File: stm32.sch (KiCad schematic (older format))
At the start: 39 parts, among them J1 USB_B_Micro, J2 Conn_02x05_Odd_Even, U1 STM32F767VITx, U5 LM2937, X1 8MHz

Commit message: manual sync & moving gerbers
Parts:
- added NT1, NT2: Net-Tie_2, rusEFI_Ola:Net-Tie_2_8.5mil, symbol Device:Net-Tie_2
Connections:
- net GND: now also NT2.2; no longer U1.36 (PB2)
- net PA9: now also NT1.2; no longer U1.68 (PA9)
- new net: NT2.1, U1.36 (PB2)
- new net: NT1.1, U1.68 (PA9)
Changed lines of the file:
@@
 Text Label 6250 3550 1    60   ~ 12
 VDD
-Text Label 7250 4750 0    60   ~ 12
+Text Label 7600 4750 0    60   ~ 12
 PA9
-Text Label 7250 4850 0    60   ~ 12
+Text Label 7600 4850 0    60   ~ 12
 PA10
-Text Label 7250 4950 0    60   ~ 12
+Text Label 7600 4950 0    60   ~ 12
 PA11
-Text Label 7250 5050 0    60   ~ 12
+Text Label 7600 5050 0    60   ~ 12
 PA12
 Wire Wire Line
@@
 	6600 2000 6600 2200
 Wire Wire Line
-	7250 5750 7950 5750
+	7250 5750 7600 5750
 Wire Wire Line
 	5100 5150 4850 5150
@@
 	6250 3550 6150 3550
 Connection ~ 6150 3550
+$Comp
+L Device:Net-Tie_2 NT2
+U 1 1 5D85D17A
+P 7700 5750
+F 0 "NT2" H 7700 5839 50  0000 C CNN
+F 1 "Net-Tie_2" H 7700 5840 50  0001 C CNN
+F 2 "rusEFI_Ola:Net-Tie_2_8.5mil" H 7700 5750 50  0001 C CNN
+F 3 "~" H 7700 5750 50  0001 C CNN
+	1    7700 5750
+	1    0    0    -1
+$EndComp
+Wire Wire Line
+	7800 5750 7950 5750
+Wire Wire Line
+	7250 4850 7600 4850
+Wire Wire Line
+	7250 4950 7600 4950
+Wire Wire Line
+	7250 5050 7600 5050
+Wire Wire Line
+	7250 4750 7300 4750
+$Comp
+L Device:Net-Tie_2 NT1
+U 1 1 5D86F689
+P 7400 4750
+F 0 "NT1" H 7400 4700 50  0000 C CNN
+F 1 "Net-Tie_2" H 7400 4840 50  0001 C CNN
+F 2 "rusEFI_Ola:Net-Tie_2_8.5mil" H 7400 4750 50  0001 C CNN
+F 3 "~" H 7400 4750 50  0001 C CNN
+	1    7400 4750
+	1    0    0    -1
+$EndComp
+Wire Wire Line
+	7500 4750 7600 4750
 $EndSCHEMATC

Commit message: Created LED footprint which better matches the MFG's suggested footprint, as well it includes a clear polarity indicator. https://github.com/rusefi/hw_microRusEfi/issues/81 Changed VVT, injector, and coil LED's to turn on when the device is being driven. https://github.com/rusefi/hw_microRusEfi/issues/82
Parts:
- D19: footprint LED_SMD:LED_0603_1608Metric -> rusEFI_Ola:LED-0603-rusEFI
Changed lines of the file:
@@
 Sheet 6 7
 Title "microRusEfi"
-Date "2019-07-01"
-Rev "R0.2"
+Date "2019-07-09"
+Rev "R0.2.1"
 Comp ""
 Comment1 ""
@@
 F 0 "D19" H 15400 3300 50  0000 C CNN
 F 1 "LED-RED" H 15300 3500 50  0000 C CNN
-F 2 "LED_SMD:LED_0603_1608Metric" H 15400 3400 60  0001 C CNN
+F 2 "rusEFI_Ola:LED-0603-rusEFI" H 15400 3400 60  0001 C CNN
 F 3 "" H 15400 3400 60  0000 C CNN
 F 4 "LTST-S270KRKT" H 0   0   50  0001 C CNN "Part #"

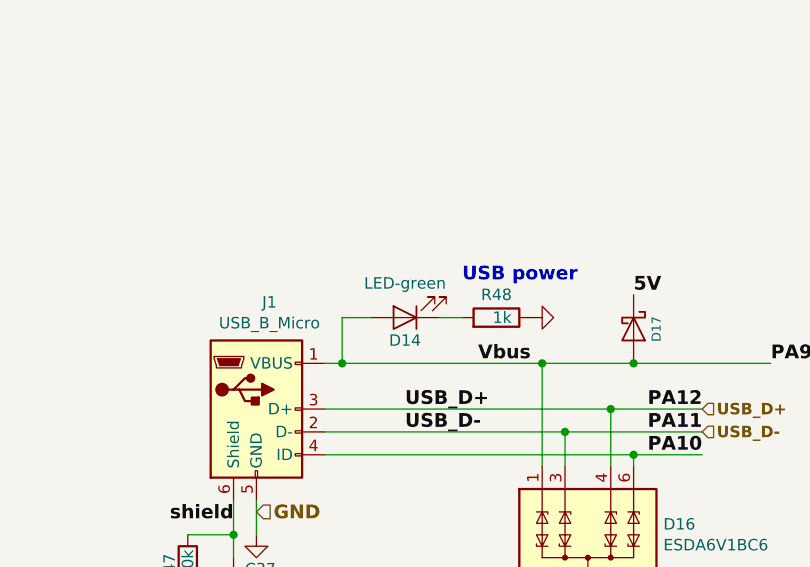
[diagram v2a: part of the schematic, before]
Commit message: Updated 1k/1.5k resistor arrays, updated 2.7k's and R141. Changed several K's into k's for consistent ref designation names. https://github.com/rusefi/hw_microRusEfi/issues/51
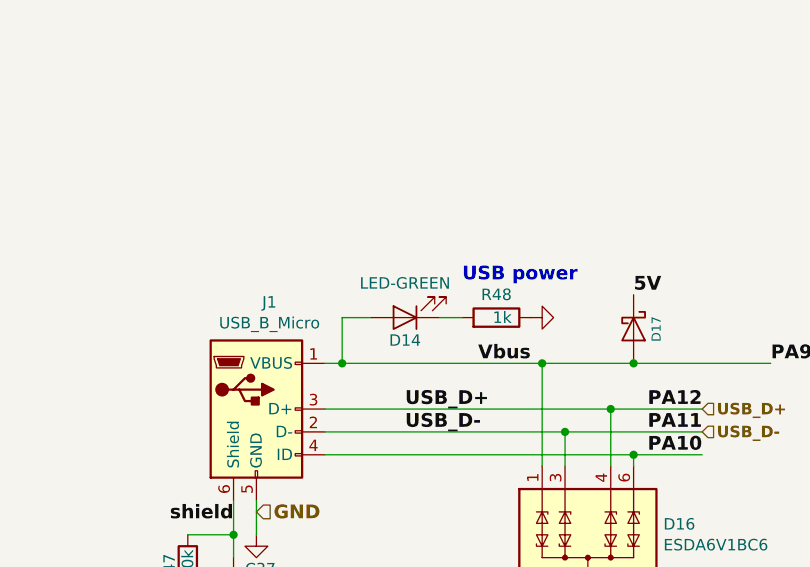
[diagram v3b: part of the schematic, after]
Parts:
- D14: value LED-green -> LED-GREEN
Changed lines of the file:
@@
 P 12150 3800
 F 0 "D14" H 12150 3900 50  0000 C CNN
-F 1 "LED-green" H 12150 3650 50  0000 C CNN
+F 1 "LED-GREEN" H 12150 3650 50  0000 C CNN
 F 2 "Capacitor_SMD:C_0603_1608Metric_Pad1.05x0.95mm_HandSolder" V 5   1700 60  0001 C CNN
 F 3 "" H 12150 3800 60  0001 C CNN
@@
 F 1 "10k" V 4050 3850 50  0000 C CNN
 F 2 "Resistor_SMD:R_0603_1608Metric" V 6380 6150 60  0001 C CNN
-F 3 "" H 9900 6175 60  0001 C CNN
+F 3 "TBD" H 9900 6175 60  0001 C CNN
 F 4 "RMCF0603JT10K0" H 0   0   50  0001 C CNN "Part #"
 F 5 "DIGI" H 0   0   50  0001 C CNN "VEND"
@@
 F 1 "10k" V 4650 4200 50  0000 C CNN
 F 2 "Resistor_SMD:R_0603_1608Metric" V 6980 6500 60  0001 C CNN
-F 3 "" H 10500 6525 60  0001 C CNN
+F 3 "TBD" H 10500 6525 60  0001 C CNN
 F 4 "RMCF0603JT10K0" H 0   0   50  0001 C CNN "Part #"
 F 5 "DIGI" H 0   0   50  0001 C CNN "VEND"

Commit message: new xtal 0.3
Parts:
- X1: footprint Crystal:Crystal_SMD_5032-2Pin_5.0x3.2mm -> Crystal_SMD_HC49-SD; Manufacturer NDK -> Abracon; Part # NX3225GD-8MHZ-STD-CRA-3 -> ABLS-8.000MHZ-B2-T; VEND# 644-1178-1-ND -> 535-9089-1-ND
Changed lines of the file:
@@
 F 0 "X1" H 4850 5450 60  0000 C CNN
 F 1 "8MHz" H 4850 5150 60  0000 C CNN
-F 2 "Crystal:Crystal_SMD_5032-2Pin_5.0x3.2mm" H 4850 5300 60  0001 C CNN
-F 3 "" H 4850 5300 60  0000 C CNN
+F 2 "Crystal_SMD_HC49-SD" H 4850 5300 60  0001 C CNN
+F 3 "" H 4850 5300 60  0001 C CNN
 F 4 "stm32f407_board" H 16200 4825 60  0001 C CNN "PageName"
 F 5 "DIGI" H -1800 1250 50  0001 C CNN "VEND"
-F 6 "NX3225GD-8MHZ-STD-CRA-3" H -1800 1250 50  0001 C CNN "Part #"
-F 7 "644-1178-1-ND" H -1800 1250 50  0001 C CNN "VEND#"
-F 8 "NDK" H 0   0   50  0001 C CNN "Manufacturer"
+F 6 "ABLS-8.000MHZ-B2-T" H -1800 1250 50  0001 C CNN "Part #"
+F 7 "535-9089-1-ND" H -1800 1250 50  0001 C CNN "VEND#"
+F 8 "Abracon " H 0   0   50  0001 C CNN "Manufacturer"
 	1    4850 5300
 	0    -1   -1   0

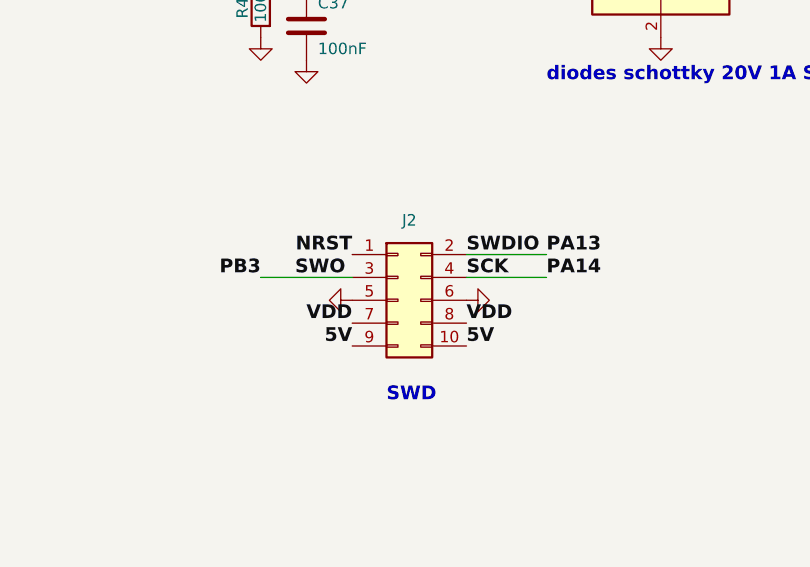
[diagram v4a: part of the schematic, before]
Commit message: Changed SWD connector to reflect validated brain board. https://github.com/rusefi/hw_microRusEfi/issues/88
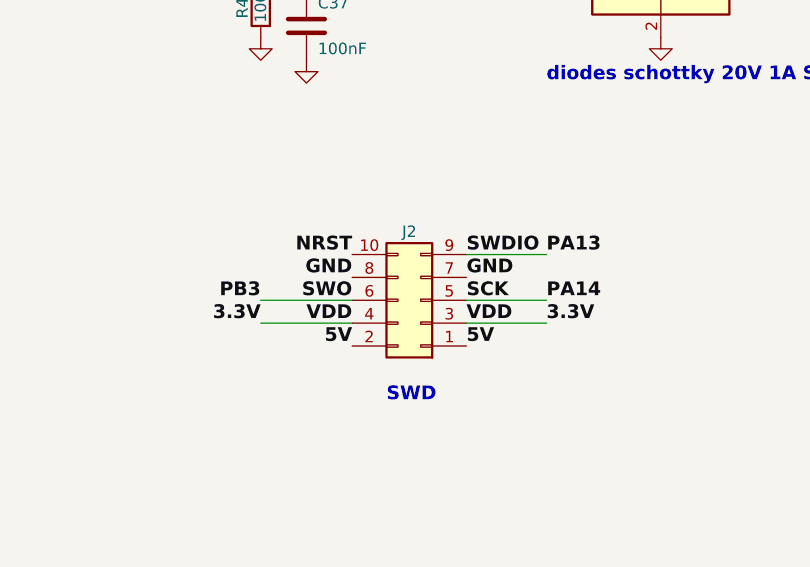
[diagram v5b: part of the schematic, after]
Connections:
- net 5V: now also J2.1 (Pin_1), J2.2 (Pin_2); no longer J2.10 (Pin_10), J2.9 (Pin_9)
- net GND: now also J2.7 (Pin_7), J2.8 (Pin_8); no longer J2.5 (Pin_5), J2.6 (Pin_6)
- net NRST: now also J2.10 (Pin_10); no longer J2.1 (Pin_1)
- net PA13: now also J2.9 (Pin_9); no longer J2.2 (Pin_2)
- net PA14: now also J2.5 (Pin_5); no longer J2.4 (Pin_4)
- net PB3: now also J2.6 (Pin_6); no longer J2.3 (Pin_3)
- net VDD: now also J2.3 (Pin_3), J2.4 (Pin_4); no longer J2.7 (Pin_7), J2.8 (Pin_8)
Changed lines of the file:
@@
 Text Notes 12400 3650 0    60   ~ 12
 USB power
-Text Label 12450 6100 0    60   ~ 12
+Text Label 12450 6200 0    60   ~ 12
 PA14
 Text Label 12450 6000 0    60   ~ 12
@@
 Text Label 11600 6000 2    60   ~ 12
 NRST
-Text Label 11200 6100 2    60   ~ 12
+Text Label 11200 6200 2    60   ~ 12
 PB3
 $Comp
@@
 	1    0    0    -1
 $EndComp
-$Comp
-L Connector_Generic:Conn_02x05_Odd_Even J2
-U 1 1 5CDE2131
-P 11800 6200
-F 0 "J2" H 11850 6550 50  0000 C CNN
-F 1 "Conn_02x05_Odd_Even" H 11850 6526 50  0001 C CNN
-F 2 "Connector_PinSocket_2.54mm:PinSocket_2x05_P2.54mm_Vertical_SMD" H 11800 6200 50  0001 C CNN
-F 3 "~" H 11800 6200 50  0001 C CNN
-F 4 "MOUSER" H 0   0   50  0001 C CNN "VEND"
-F 5 "Amphenol" H 0   0   50  0001 C CNN "Manufacturer"
-F 6 "95278-801B10LF" H 0   0   50  0001 C CNN "Part #"
-F 7 "649-95278-801B10LF" H 0   0   50  0001 C CNN "VEND#"
-	1    11800 6200
-	1    0    0    -1
-$EndComp
 Text Label 12100 6000 0    60   ~ 12
 SWDIO
 Wire Wire Line
-	12100 6100 12450 6100
-$Comp
-L power:GND #PWR0145
-U 1 1 5CDFAB3E
-P 12100 6200
-F 0 "#PWR0145" H 12100 6200 30  0001 C CNN
-F 1 "GND" H 12100 6130 30  0001 C CNN
-F 2 "" H 12100 6200 60  0000 C CNN
-F 3 "" H 12100 6200 60  0000 C CNN
-	1    12100 6200
-	0    -1   -1   0
-$EndComp
-$Comp
-L power:GND #PWR0146
-U 1 1 5CDFB72E
-P 11600 6200
-F 0 "#PWR0146" H 11600 6200 30  0001 C CNN
-F 1 "GND" H 11600 6130 30  0001 C CNN
-F 2 "" H 11600 6200 60  0000 C CNN
-F 3 "" H 11600 6200 60  0000 C CNN
-	1    11600 6200
-	0    1    1    0
-$EndComp
+	12100 6200 12450 6200
 Wire Wire Line
 	12100 6000 12450 6000
-Text Label 12100 6100 0    60   ~ 12
+Text Label 12100 6200 0    60   ~ 12
 SCK
-Text Label 11350 6100 0    60   ~ 12
+Text Label 11600 6200 2    60   ~ 12
 SWO
 Text Label 11600 6300 2    60   ~ 12
 VDD
-Wire Wire Line
-	11600 6100 11200 6100
 Text Label 11600 6400 2    60   ~ 12
 5V
@@
 Wire Wire Line
 	7500 4750 7600 4750
+Wire Wire Line
+	11600 6200 11200 6200
+$Comp
+L Connector_Generic:Conn_02x05_Odd_Even J2
+U 1 1 5CDE2131
+P 11900 6200
+F 0 "J2" H 11950 5900 50  0000 C CNN
+F 1 "Conn_02x05_Odd_Even" H 11950 6526 50  0001 C CNN
+F 2 "Connector_PinSocket_2.54mm:PinSocket_2x05_P2.54mm_Vertical_SMD" H 11900 6200 50  0001 C CNN
+F 3 "~" H 11900 6200 50  0001 C CNN
+F 4 "MOUSER" H 100 0   50  0001 C CNN "VEND"
+F 5 "Amphenol" H 100 0   50  0001 C CNN "Manufacturer"
+F 6 "95278-801B10LF" H 100 0   50  0001 C CNN "Part #"
+F 7 "649-95278-801B10LF" H 100 0   50  0001 C CNN "VEND#"
+	1    11900 6200
+	-1   0    0    1
+$EndComp
+Text Label 11600 6100 2    60   ~ 12
+GND
+Text Label 12100 6100 0    60   ~ 12
+GND
+Text Label 12450 6300 0    60   ~ 12
+3.3V
+Wire Wire Line
+	12100 6300 12450 6300
+Text Label 11200 6300 2    60   ~ 12
+3.3V
+Wire Wire Line
+	11600 6300 11200 6300
 $EndSCHEMATC

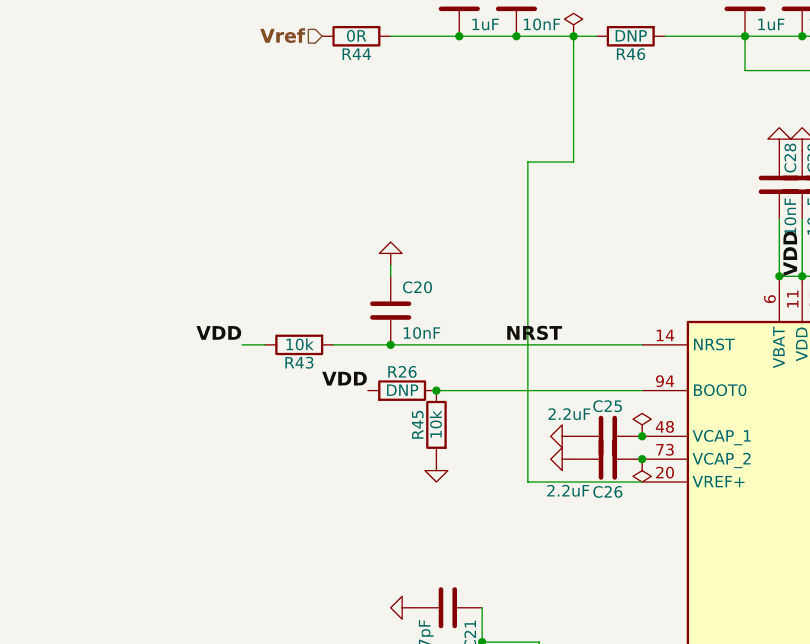
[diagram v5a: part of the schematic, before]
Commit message: Changed R26 into push button SW1 BOM is still TBD https://github.com/rusefi/hw_microRusEfi/issues/86
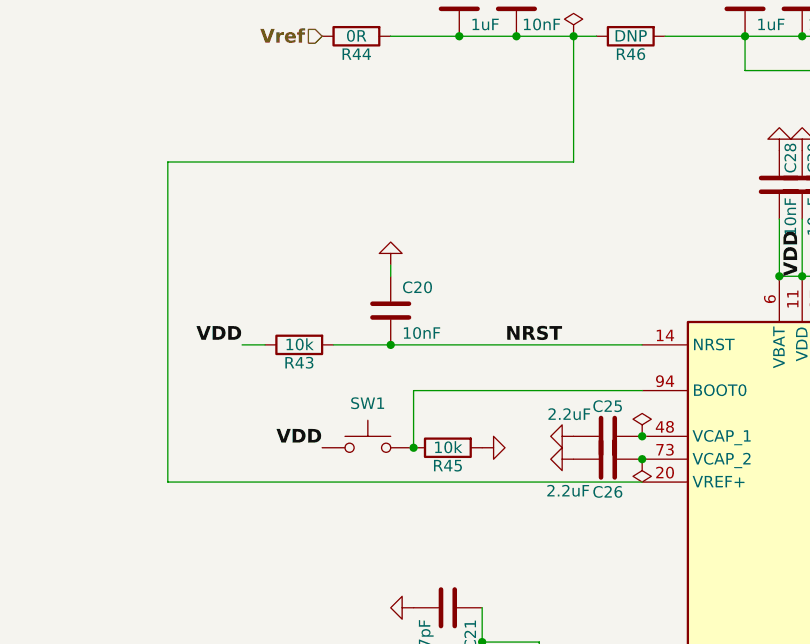
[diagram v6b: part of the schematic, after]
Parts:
- removed R26: DNP, Resistor_SMD:R_0603_1608Metric, symbol Device:R
- added SW1: SW_Push, Button_Switch_SMD:SW_SPST_B3U-1000P, symbol Switch:SW_Push
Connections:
- net VDD: now also SW1.1
- net at R45.1, U1.94 (BOOT0): now also SW1.2
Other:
- moved on the sheet: R45
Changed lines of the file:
@@
 L Device:R R45
 U 1 1 5CC9138A
-P 4650 4200
-F 0 "R45" V 4730 4200 50  0000 C CNN
-F 1 "10k" V 4650 4200 50  0000 C CNN
-F 2 "Resistor_SMD:R_0603_1608Metric" V 6980 6500 60  0001 C CNN
-F 3 "TBD" H 10500 6525 60  0001 C CNN
-F 4 "RMCF0603JT10K0" H 0   0   50  0001 C CNN "Part #"
-F 5 "DIGI" H 0   0   50  0001 C CNN "VEND"
-F 6 "RMCF0603JT10K0CT-ND" H 0   0   50  0001 C CNN "VEND#"
-F 7 "StackPole" H 0   0   50  0001 C CNN "Manufacturer"
-	1    4650 4200
-	-1   0    0    -1
+P 4700 4300
+F 0 "R45" V 4780 4300 50  0000 C CNN
+F 1 "10k" V 4700 4300 50  0000 C CNN
+F 2 "Resistor_SMD:R_0603_1608Metric" V 7030 6600 60  0001 C CNN
+F 3 "TBD" H 10550 6625 60  0001 C CNN
+F 4 "RMCF0603JT10K0" H 50  100 50  0001 C CNN "Part #"
+F 5 "DIGI" H 50  100 50  0001 C CNN "VEND"
+F 6 "RMCF0603JT10K0CT-ND" H 50  100 50  0001 C CNN "VEND#"
+F 7 "StackPole" H 50  100 50  0001 C CNN "Manufacturer"
+	1    4700 4300
+	0    -1   1    0
 $EndComp
 Text Label 5200 3850 2    60   ~ 12
@@
 	5100 5450 4850 5450
 Connection ~ 4850 5450
-Wire Wire Line
-	5550 4050 4650 4050
 $Comp
 L power:GND #PWR0190
 U 1 1 5CFE03F2
-P 4650 4350
-F 0 "#PWR0190" H 4650 4350 30  0001 C CNN
-F 1 "GND" H 4650 4280 30  0001 C CNN
-F 2 "" H 4650 4350 60  0001 C CNN
-F 3 "" H 4650 4350 60  0001 C CNN
-	1    4650 4350
-	1    0    0    -1
-$EndComp
-Wire Wire Line
-	5550 4450 5050 4450
+P 4850 4300
+F 0 "#PWR0190" H 4850 4300 30  0001 C CNN
+F 1 "GND" H 4850 4230 30  0001 C CNN
+F 2 "" H 4850 4300 60  0001 C CNN
+F 3 "" H 4850 4300 60  0001 C CNN
+	1    4850 4300
+	0    -1   -1   0
+$EndComp
 Wire Wire Line
 	6150 3300 6150 3550
@@
 	6650 3300 6650 3550
 Wire Wire Line
-	5050 3050 5250 3050
+	3475 3050 5250 3050
 $Comp
 L MCU_ST_STM32F7:STM32F767VITx U1
@@
 $EndComp
 Wire Wire Line
-	5050 3050 5050 4450
+	3475 3050 3475 4450
 Wire Wire Line
 	4200 3850 4450 3850
@@
 	15350 3175 15200 3175
 Connection ~ 15200 3175
-$Comp
-L Device:R R26
-U 1 1 5D13DF09
-P 4500 4050
-F 0 "R26" V 4580 4050 50  0000 C CNN
-F 1 "DNP" V 4500 4050 50  0000 C CNN
-F 2 "Resistor_SMD:R_0603_1608Metric" V 6830 6350 60  0001 C CNN
-F 3 "" H 10350 6375 60  0001 C CNN
-F 4 "DNP" H 0   0   50  0001 C CNN "Part #"
-F 5 "DIGI" H 0   0   50  0001 C CNN "VEND"
-F 6 "DNP" H 0   0   50  0001 C CNN "VEND#"
-F 7 "DNP" H 0   0   50  0001 C CNN "Manufacturer"
-	1    4500 4050
-	0    1    -1   0
-$EndComp
-Connection ~ 4650 4050
-Text Label 4350 4050 2    60   ~ 12
+Text Label 4150 4300 2    60   ~ 12
 VDD
 $Comp
@@
 Wire Wire Line
 	11600 6300 11200 6300
+$Comp
+L Switch:SW_Push SW1
+U 1 1 5D4BAD74
+P 4350 4300
+F 0 "SW1" H 4350 4493 50  0000 C CNN
+F 1 "SW_Push" H 4350 4494 50  0001 C CNN
+F 2 "Button_Switch_SMD:SW_SPST_B3U-1000P" H 4350 4500 50  0001 C CNN
+F 3 "~" H 4350 4500 50  0001 C CNN
+F 4 "TBD" H 0   0   50  0001 C CNN "Manufacturer"
+F 5 "TBD" H 0   0   50  0001 C CNN "Part #"
+F 6 "DIGI" H 0   0   50  0001 C CNN "VEND"
+F 7 "TBD" H 0   0   50  0001 C CNN "VEND#"
+	1    4350 4300
+	1    0    0    -1
+$EndComp
+Wire Wire Line
+	4550 4300 4550 4050
+Wire Wire Line
+	4550 4050 5550 4050
+Connection ~ 4550 4300
+Wire Wire Line
+	3475 4450 5550 4450
 $EndSCHEMATC

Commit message: Changed footprint for slightly larger push button https://github.com/rusefi/hw_microRusEfi/issues/86
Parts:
- SW1: footprint Button_Switch_SMD:SW_SPST_B3U-1000P -> Button_Switch_SMD:SW_Push_SPST_NO_Alps_SKRK
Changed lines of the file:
@@
 F 0 "SW1" H 4350 4493 50  0000 C CNN
 F 1 "SW_Push" H 4350 4494 50  0001 C CNN
-F 2 "Button_Switch_SMD:SW_SPST_B3U-1000P" H 4350 4500 50  0001 C CNN
+F 2 "Button_Switch_SMD:SW_Push_SPST_NO_Alps_SKRK" H 4350 4500 50  0001 C CNN
 F 3 "~" H 4350 4500 50  0001 C CNN
 F 4 "TBD" H 0   0   50  0001 C CNN "Manufacturer"

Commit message: DRAFT
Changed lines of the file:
@@
 Text Label 11600 6000 2    60   ~ 12
 NRST
-Text Label 11200 6200 2    60   ~ 12
+Text Label 10900 6200 2    60   ~ 12
 PB3
 $Comp
@@
 	7500 4750 7600 4750
 Wire Wire Line
-	11600 6200 11200 6200
+	11600 6200 10900 6200
 $Comp
 L Connector_Generic:Conn_02x05_Odd_Even J2
@@
 Wire Wire Line
 	12100 6300 12450 6300
-Text Label 11200 6300 2    60   ~ 12
+Text Label 10900 6300 2    60   ~ 12
 3.3V
 Wire Wire Line
-	11600 6300 11200 6300
+	11600 6300 10900 6300
 $Comp
 L Switch:SW_Push SW1
@@
 Wire Wire Line
 	3475 4450 5550 4450
+Text Label 11350 6200 2    60   ~ 12
+SWIM
+Wire Notes Line
+	11700 6125 11725 6125
+Wire Notes Line
+	11725 6125 11725 6275
+Wire Notes Line
+	11725 6275 11700 6275
+Wire Notes Line
+	11700 6275 11700 6125
 $EndSCHEMATC
